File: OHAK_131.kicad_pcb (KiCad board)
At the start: 4 copper layers, 38.1 x 25.4 mm, 52 parts, among them P1 CONN_01X10, P2 USB_OTG, U1 rfd_77101, U2 MAX30100, U3 MIC5365-X.XYMT-TZ, U4 BMI160, U5 MCP73831, U6 MIC5365-X.XYMT-TZ, U7 TXS0102_LEVEL_SHIFTER_X2SON8, U8 MAX809

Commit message: Moving things around
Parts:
- C14, R7, R8: moved to F.Cu
- moved R15 12.2 mm to (125.0, 97.2), turned to 180 degrees
- moved R13 10.9 mm to (125.1, 92.8)
- moved D3 4.97 mm to (130.1, 95.3)
- moved U5 1.87 mm to (133.0, 93.7)
- moved R8 1.66 mm to (138.0, 93.6)
- moved R7 1.63 mm to (138.0, 94.5)
- moved R14 1.59 mm to (130.2, 92.5), turned to 180 degrees
- moved C14 0.51 mm to (138.0, 92.7), turned to 0 degrees
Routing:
- net Net-(R13-Pad1): track 13.3 -> 0.00 mm, vias 2 -> 0
- net GND: track 66.9 -> 57.6 mm, vias 8 -> 7
- net Net-(D3-Pad3): track 5.61 -> 0.00 mm
- net /V_SENSE: track 10.3 -> 5.06 mm, vias 1 -> 0
- net Net-(D3-Pad4): track 3.66 -> 0.00 mm
- net Net-(BT1-Pad1): track 12.6 -> 10.8 mm
- net VPP: track 39.5 -> 37.8 mm
- net Net-(R14-Pad1): track 1.66 -> 0.00 mm
- net Net-(D3-Pad1): track 1.56 -> 0.00 mm
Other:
- rule trace_min: 0.2 -> 0.18

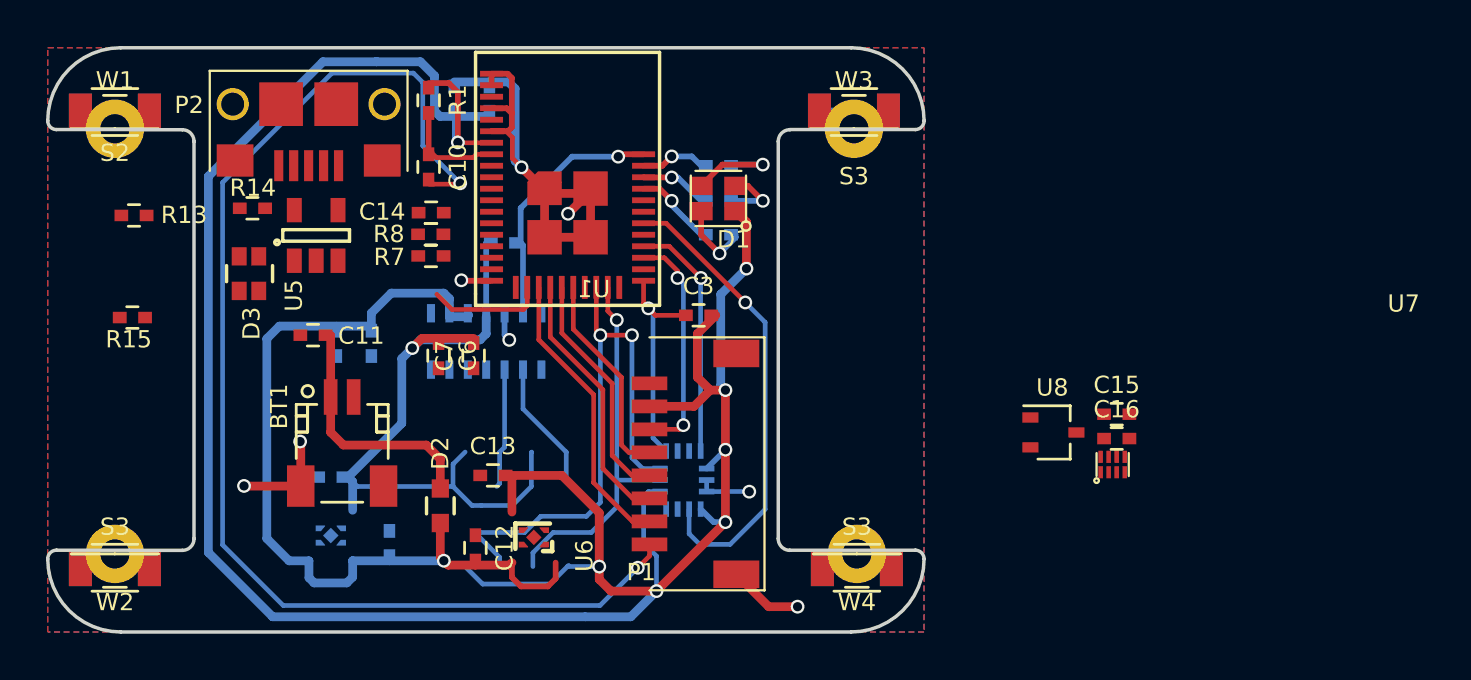
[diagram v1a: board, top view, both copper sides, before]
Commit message: moved parts to top layer and routed board
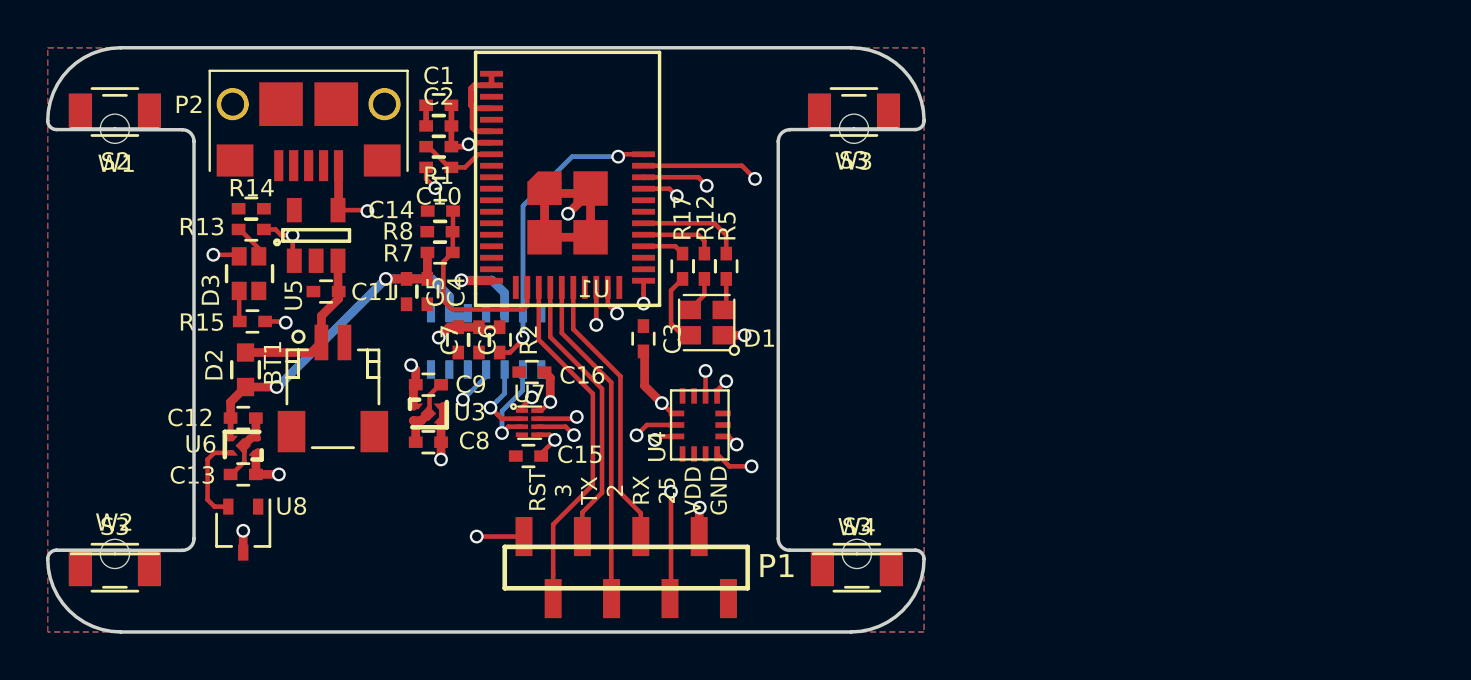
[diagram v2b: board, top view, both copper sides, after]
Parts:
- C1, C2, C4, C5, C8, C9, R12, R17, R2, R5, U3, U4: moved to F.Cu
- P1: value CONN_01X10 -> CONN_01X08; footprint Solutions:4u-0201GDVE06 -> Solutions:M50-3140845_1x8_SMT_F
- moved U8 35.5 mm to (129.8, 106.4), turned to 270 degrees
- moved C15 25.6 mm to (142.2, 103.2)
- moved C16 25.6 mm to (142.4, 99.6)
- moved U7 25.4 mm to (142.3, 101.8), turned to 270 degrees
- moved U6 13.2 mm to (129.8, 102.8)
- moved C12 11.6 mm to (129.8, 101.6), turned to 180 degrees
- moved C13 10.9 mm to (129.8, 104.0)
- moved D2 10.3 mm to (129.9, 99.5)
- moved U3 6.79 mm to (137.9, 101.4), turned to 270 degrees
- moved C9 5.84 mm to (137.9, 100.1), turned to 180 degrees
- moved D1 5.42 mm to (150.0, 97.4)
- moved R15 5.22 mm to (130.2, 97.4)
- moved R13 5.14 mm to (130.2, 93.4)
- moved C8 4.72 mm to (137.9, 102.6), turned to 0 degrees
- moved R12 4.41 mm to (149.9, 95.0), turned to 90 degrees
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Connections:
- BT1 pad : (no net) -> GND
- C8 pad 2: VPP -> VDD
- P1 pad 6: /PIN_4 -> /PIN_25
- P2 pad 10: (no net) -> GND
- P2 pad 11: (no net) -> GND
- P2 pad 7: (no net) -> GND
- P2 pad 8: (no net) -> GND
- P2 pad 9: (no net) -> GND
- U1 pad 32: /PIN_4 -> Net-(U1-Pad32)
- U1 pad 33: /BMI_INT1 -> /B_LED
- U1 pad 34: Net-(U1-Pad34) -> /G_LED
- U1 pad 35: /BMI_INT2 -> /R_LED
- U1 pad 38: /B_LED -> /PIN_25
- U1 pad 39: /R_LED -> /BMI_INT2
- U1 pad 40: /G_LED -> /BMI_INT1
- U3 pad 3: VPP -> VDD
- U3 pad 4: /EN -> VDD
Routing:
- net VDD: track 111.8 -> 17.2 mm, vias 7 -> 9
- net Net-(C10-Pad2): track 54.1 -> 19.0 mm
- net GND: track 57.6 -> 30.5 mm, vias 7 -> 4
- net +1V8: track 30.6 -> 7.31 mm, vias 1 -> 4
- net /PIN_25: track 0.00 -> 19.2 mm, vias 0 -> 2
- net /3V3_SDA: track 25.5 -> 12.8 mm, vias 2 -> 3
- net Net-(D3-Pad3): track 0.00 -> 11.9 mm, vias 0 -> 2
- net VPP: track 37.8 -> 26.2 mm, vias 1 -> 3
- net /PIN_4: track 10.1 -> 0.00 mm, vias 2 -> 0
- net /BMI_INT1: track 10.6 -> 19.6 mm, vias 1 -> 2
- net /BMI_INT2: track 20.4 -> 12.1 mm, vias 1 -> 2
- net Net-(R13-Pad1): track 0.00 -> 7.34 mm, vias 0 -> 2
- net (no net): track 4.42 -> 0.00 mm, vias 2 -> 0
- net /PIN_2: track 10.2 -> 14.4 mm
- net /EN: track 0.00 -> 3.79 mm
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- added copper zone on B.Cu, net +1V8
- added copper zone on In2.Cu, net GND
- added copper zone on In1.Cu, net VDD
- removed copper zone on B.Cu, net GND
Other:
- net class TINY_PADS: trace_width 0.25 -> 0.2
- board text added: "20 x 25 battery"
- board text added: "RST 3 TX 2 RX 25 VDD GND"

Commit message: tidying up a bit
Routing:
- net GND: track 30.5 -> 32.4 mm
- net Net-(R14-Pad1): track 0.00 -> 1.34 mm
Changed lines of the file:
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@@
     (thickness 1.6)
     (drawings 53)
-    (tracks 315)
+    (tracks 321)
     (zones 0)
     (modules 52)
@@
   (page A4)
   (layers
-    (0 F.Cu signal)
-    (1 In1.Cu signal)
-    (2 In2.Cu signal)
+    (0 F.Cu signal hide)
+    (1 In1.Cu signal hide)
+    (2 In2.Cu signal hide)
     (31 B.Cu signal)
     (32 B.Adhes user)
@@
     (37 F.SilkS user)
     (38 B.Mask user)
-    (39 F.Mask user)
-    (40 Dwgs.User user hide)
+    (39 F.Mask user hide)
+    (40 Dwgs.User user)
     (41 Cmts.User user hide)
     (42 Eco1.User user hide)
@@
   )
   (setup
-    (last_trace_width 0.381)
+    (last_trace_width 0.2032)
     (user_trace_width 0.18)
     (user_trace_width 0.2)
@@
     (aux_axis_origin 121.34088 110.89386)
     (grid_origin 121.34088 110.89386)
-    (visible_elements FFFFFFFF)
+    (visible_elements FFFF7FFF)
     (pcbplotparams
       (layerselection 0x010fc_80000001)
@@
     (tags "capacitor 0402")
     (attr smd)
-    (fp_text reference C7 (at 0 -1.27 90) (layer F.SilkS)
+    (fp_text reference C7 (at 0 2.2 90) (layer F.SilkS)
       (effects (font (size 0.75 0.75) (thickness 0.15)))
     )
@@
     (tags "capacitor 0603")
     (attr smd)
-    (fp_text reference D2 (at 0.2 -1.35 90) (layer F.SilkS)
+    (fp_text reference D2 (at -0.55 -1.35 90) (layer F.SilkS)
       (effects (font (size 0.75 0.75) (thickness 0.15)))
     )
@@
     (tags "capacitor 0402")
     (attr smd)
-    (fp_text reference C1 (at 0 -1.27) (layer F.SilkS)
+    (fp_text reference C1 (at 0 -1.8) (layer F.SilkS)
       (effects (font (size 0.75 0.75) (thickness 0.15)))
     )
@@
     (tags "capacitor 0402")
     (attr smd)
-    (fp_text reference C2 (at 0 -1.27) (layer F.SilkS)
+    (fp_text reference C2 (at 0 -1.85) (layer F.SilkS)
       (effects (font (size 0.75 0.75) (thickness 0.15)))
     )
@@
     (tags "capacitor 0402")
     (attr smd)
-    (fp_text reference C4 (at 0 -1.27 270) (layer F.SilkS)
+    (fp_text reference C4 (at 0 -1.1 270) (layer F.SilkS)
       (effects (font (size 0.75 0.75) (thickness 0.15)))
     )
@@
     (tags "capacitor 0402")
     (attr smd)
-    (fp_text reference C5 (at 0 -1.27 270) (layer F.SilkS)
+    (fp_text reference C5 (at 1.8 -0.05 270) (layer F.SilkS)
       (effects (font (size 0.75 0.75) (thickness 0.15)))
     )
@@
     (tags "capacitor 0402")
     (attr smd)
-    (fp_text reference C6 (at 0 -1.27 270) (layer F.SilkS)
+    (fp_text reference C6 (at 0 -4.2 270) (layer F.SilkS)
       (effects (font (size 0.75 0.75) (thickness 0.15)))
     )
@@
     (tags "capacitor 0402")
     (attr smd)
-    (fp_text reference C10 (at 0 -1.27 180) (layer F.SilkS)
+    (fp_text reference C10 (at -0.05 -1 180) (layer F.SilkS)
       (effects (font (size 0.75 0.75) (thickness 0.15)))
     )
@@
     (tags "capacitor 0402")
     (attr smd)
-    (fp_text reference C12 (at 2.3 0 180) (layer F.SilkS)
+    (fp_text reference C12 (at 1.5 -0.3 270) (layer F.SilkS)
       (effects (font (size 0.75 0.75) (thickness 0.15)))
     )
@@
     (tags "capacitor 0402")
     (attr smd)
-    (fp_text reference C13 (at -2.2 0.05) (layer F.SilkS)
+    (fp_text reference C13 (at 2.2 0.1) (layer F.SilkS)
       (effects (font (size 0.75 0.75) (thickness 0.15)))
     )
@@
     (tags "capacitor 0402")
     (attr smd)
-    (fp_text reference R1 (at 0 -1.27 180) (layer F.SilkS)
+    (fp_text reference R1 (at 1.8 -1.85 180) (layer F.SilkS)
       (effects (font (size 0.75 0.75) (thickness 0.15)))
     )
@@
     (tags "capacitor 0402")
     (attr smd)
-    (fp_text reference R2 (at 0 -1.27 270) (layer F.SilkS)
+    (fp_text reference R2 (at 0 -3.7 270) (layer F.SilkS)
       (effects (font (size 0.75 0.75) (thickness 0.15)))
     )
@@
     (tags "capacitor 0402")
     (attr smd)
-    (fp_text reference R13 (at 2.15 0.1 180) (layer F.SilkS)
+    (fp_text reference R13 (at 1.75 0 270) (layer F.SilkS)
       (effects (font (size 0.75 0.75) (thickness 0.15)))
     )
@@
     (tags "capacitor 0402")
     (attr smd)
-    (fp_text reference R15 (at 2.2 -0.05 180) (layer F.SilkS)
+    (fp_text reference R15 (at 1.7 -0.5 270) (layer F.SilkS)
       (effects (font (size 0.75 0.75) (thickness 0.15)))
     )
@@
   (module "Solutions:MLF-4 1mm x 1mm" (layer F.Cu)
     (at 129.84088 102.79386 90)
-    (fp_text reference U6 (at 0.05 -1.85 180) (layer F.SilkS)
+    (fp_text reference U6 (at -0.95 -1.45 270) (layer F.SilkS)
       (effects (font (size 0.75 0.75) (thickness 0.15)))
     )
@@
   (gr_line (start 139.94088 99.69386) (end 139.94088 85.69386) (layer Cmts.User) (width 0.2))
   (gr_line (start 149.94088 99.69386) (end 139.94088 99.69386) (layer Cmts.User) (width 0.2))
-  (gr_text "RST\n3\nTX\n2\nRX\n25\nVDD\nGND" (at 146.59088 104.74386 90) (layer F.SilkS)
-    (effects (font (size 0.7 0.7) (thickness 0.15)))
+  (gr_text "RST\n3\nTX\n2\nRX\n25\nVDD\nGND" (at 146.54088 106.79386 90) (layer B.SilkS)
+    (effects (font (size 0.7 0.7) (thickness 0.15)) (justify mirror))
   )
   (gr_line (start 152.14088 109.09386) (end 141.54088 109.09386) (layer Eco1.User) (width 0.2))
@@
   (segment (start 140.40388 99.78086) (end 139.39088 100.79386) (width 0.2) (layer B.Cu) (net 1))
   (segment (start 140.40388 99.33686) (end 140.40388 99.78086) (width 0.2) (layer B.Cu) (net 1))
+  (segment (start 142.66088 91.54886) (end 142.94088 91.82886) (width 0.2) (layer F.Cu) (net 1))
+  (segment (start 142.66088 91.10386) (end 142.66088 91.54886) (width 0.2) (layer F.Cu) (net 1))
+  (segment (start 141.95588 102.97886) (end 141.69088 103.24386) (width 0.2032) (layer F.Cu) (net 1))
+  (segment (start 141.95588 102.31886) (end 141.95588 102.97886) (width 0.2032) (layer F.Cu) (net 1))
   (segment (start 138.89088 87.99386) (end 138.89088 88.89386) (width 0.25) (layer F.Cu) (net 2))
   (segment (start 138.89088 89.79386) (end 138.89088 88.89386) (width 0.25) (layer F.Cu) (net 2))
@@
   (segment (start 131.24088 93.39386) (end 131.49088 93.64386) (width 0.2) (layer F.Cu) (net 45))
   (segment (start 130.74088 93.39386) (end 131.24088 93.39386) (width 0.2) (layer F.Cu) (net 45))
+  (segment (start 132.00088 92.49386) (end 132.06088 92.55386) (width 0.2032) (layer F.Cu) (net 46))
+  (segment (start 130.74088 92.49386) (end 132.00088 92.49386) (width 0.2032) (layer F.Cu) (net 46))
   (segment (start 137.24088 100.24386) (end 137.34088 100.14386) (width 0.381) (layer F.Cu) (net 48))
   (segment (start 137.24088 101.081361) (end 137.24088 100.24386) (width 0.381) (layer F.Cu) (net 48))

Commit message: finish tidying up
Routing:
- net GND: track 32.4 -> 33.4 mm, vias 4 -> 5
- net VDD: track 17.2 -> 17.8 mm
